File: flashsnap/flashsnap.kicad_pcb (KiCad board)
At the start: 2 copper layers, 28 x 25 mm, 9 parts, among them CON1 BARREL_JACK, P1 CONN_10, P2 CONN_10, Q1 NPN, Q2 NPN, SW1 SWITCH_INV

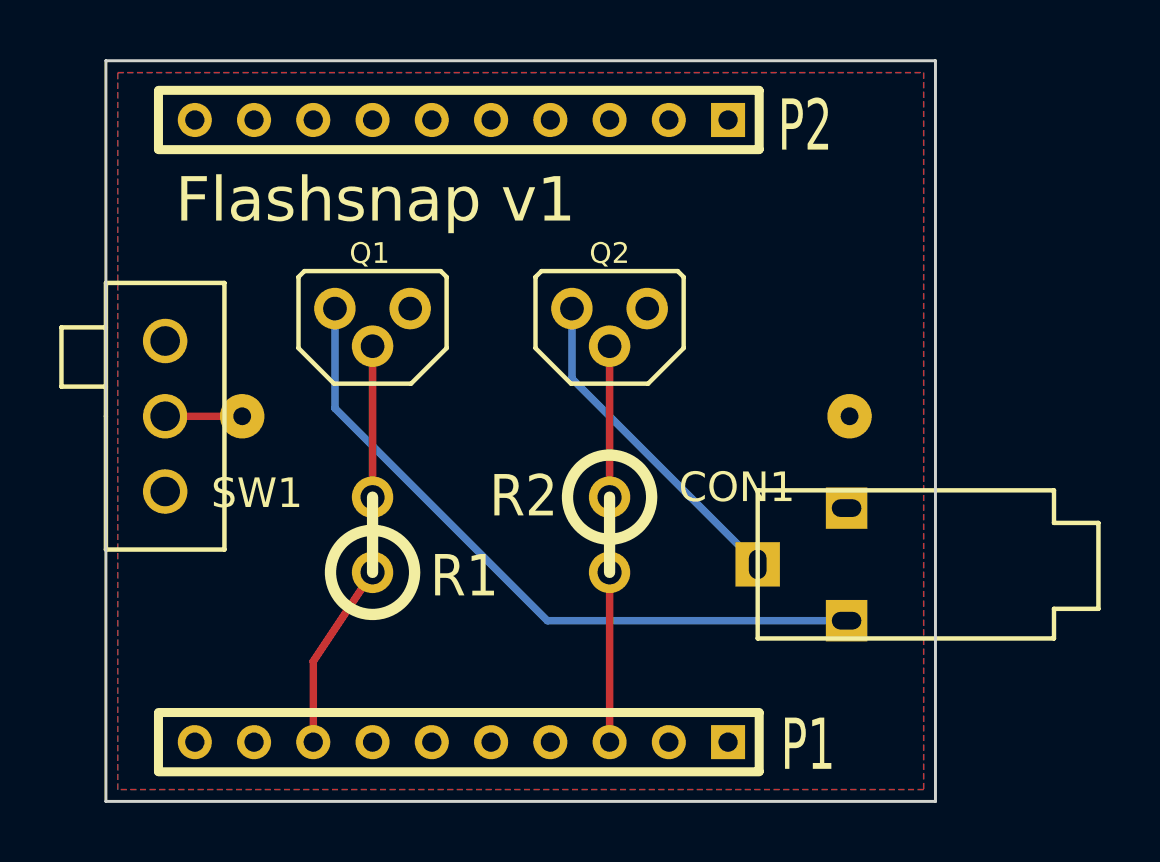
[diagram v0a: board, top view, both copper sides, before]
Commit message: flashsnap: Update main board, add manual and lightning trigger shields
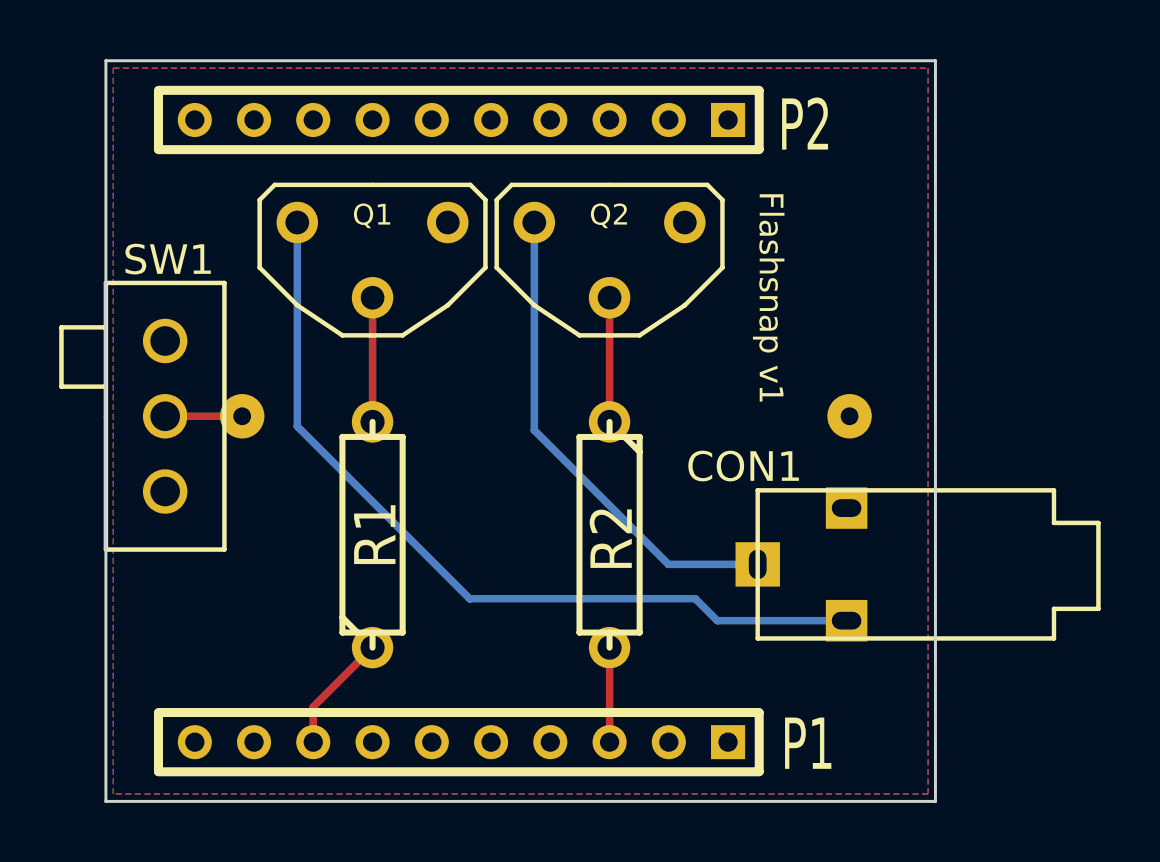
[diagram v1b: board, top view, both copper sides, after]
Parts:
- Q1, Q2: footprint TO92PN -> TO92PN-LARGE
- R1, R2: footprint R1 -> R3
- moved Q1 1.00 mm to (189.0, 143.0)
- moved Q2 1.00 mm to (197.0, 143.0)
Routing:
- net N-0000010: track 11.2 -> 16.4 mm
- net N-0000011: track 23.6 -> 28.1 mm
- net N-000008: track 5.73 -> 3.19 mm
- net N-0000012: track 6.34 -> 4.02 mm
- net N-000009: track 5.09 -> 3.56 mm
- net N-000007: track 5.09 -> 3.56 mm

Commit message: flashsnap: Introduce cable-shield, update others.
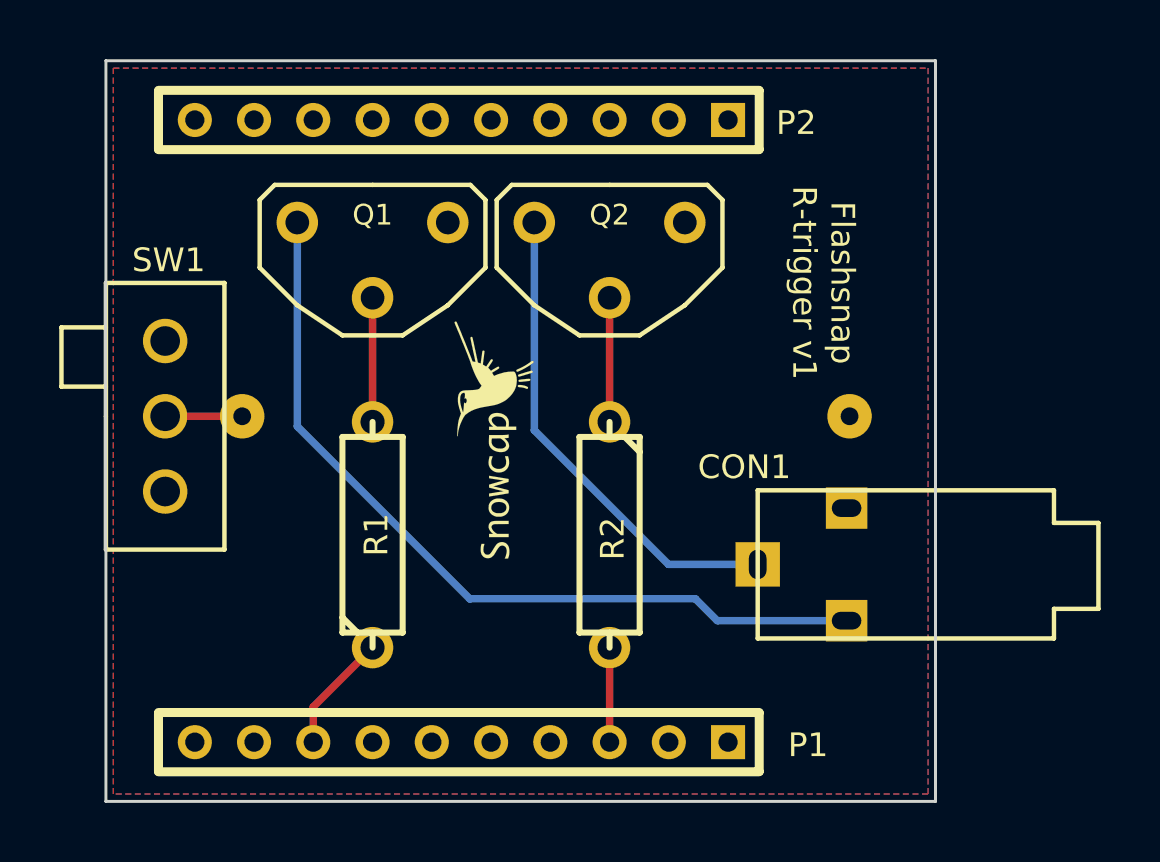
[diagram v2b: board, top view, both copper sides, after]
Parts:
- added VAL: REF, LOGO_SMALL_SNOWCAP_FRONT, F.Cu at (193.1, 147.8)
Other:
- board text added: "Flashsnap R-trigger v1"
- board text removed: "Flashsnap v1"
